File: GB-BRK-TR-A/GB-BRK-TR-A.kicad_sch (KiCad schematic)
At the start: 7 parts

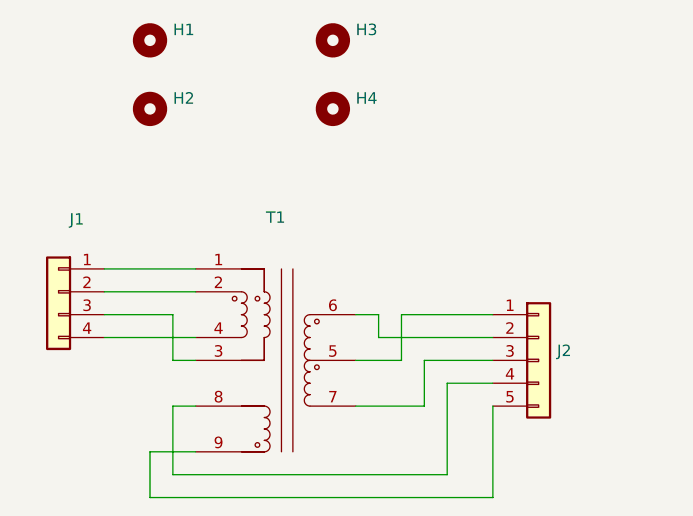
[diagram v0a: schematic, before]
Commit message: Upgrade projects to KiCad 7
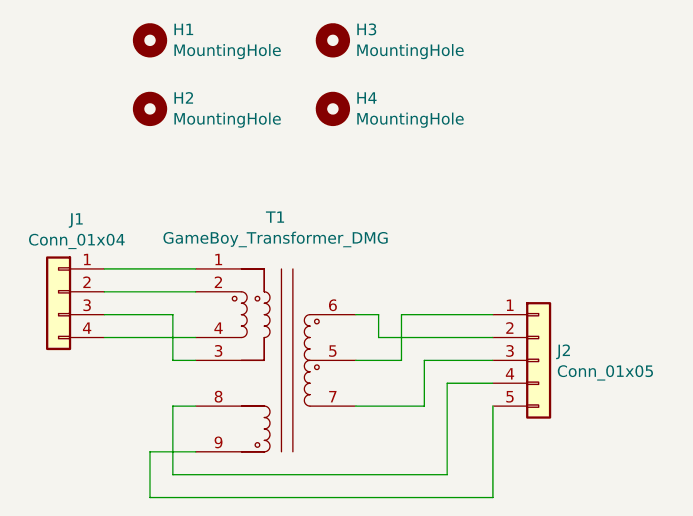
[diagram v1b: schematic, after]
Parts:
- H1, H2, H3, H4: value (none) -> MountingHole; footprint (none) -> MountingHole:MountingHole_3.2mm_M3
- J1: value (none) -> Conn_01x04; footprint (none) -> Connector_PinHeader_2.54mm:PinHeader_1x04_P2.54mm_Vertical
- J2: value (none) -> Conn_01x05; footprint (none) -> Connector_PinHeader_2.54mm:PinHeader_1x05_P2.54mm_Vertical
- T1: value (none) -> GameBoy_Transformer_DMG; footprint (none) -> Gekkio_Transformer_THT:Transformer_GameBoy_DMG
